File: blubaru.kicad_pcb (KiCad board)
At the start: 2 copper layers, 64 parts, among them IC1 ATTINY4313-P, J1 DB15, J2 DB15, J3 TS5A22364-Q1, J4 TS5A22364-Q1, J5 RN52_BREAKOUT, J6 JACK_TRS_5PINS, J7 DRV632, J8 JACK_TRS_5PINS, P1 CONN_01X06, P2 CONN_02X03, SW1 SW_Push, U1 DG419, U2 LD1117V33, Y1 11.0592MHz

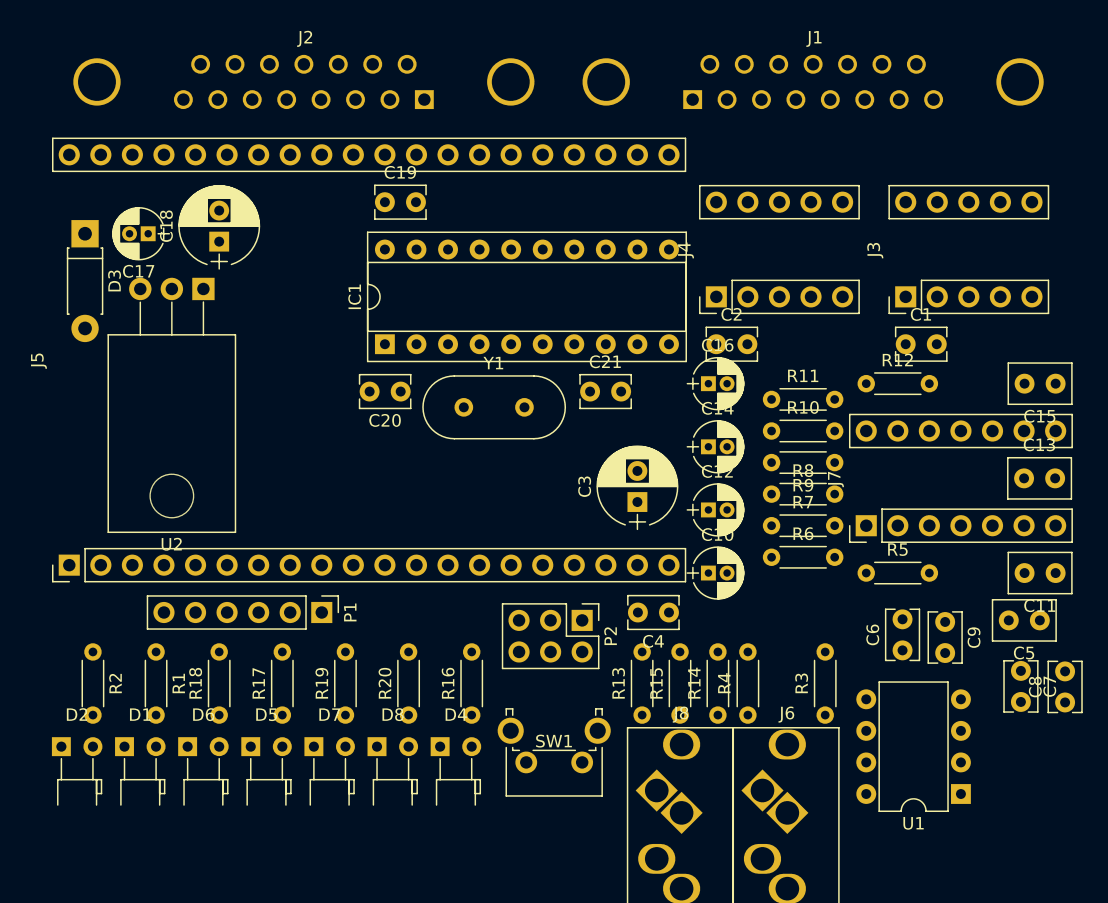
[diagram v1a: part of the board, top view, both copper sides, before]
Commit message: Add a better footprint for the regulator
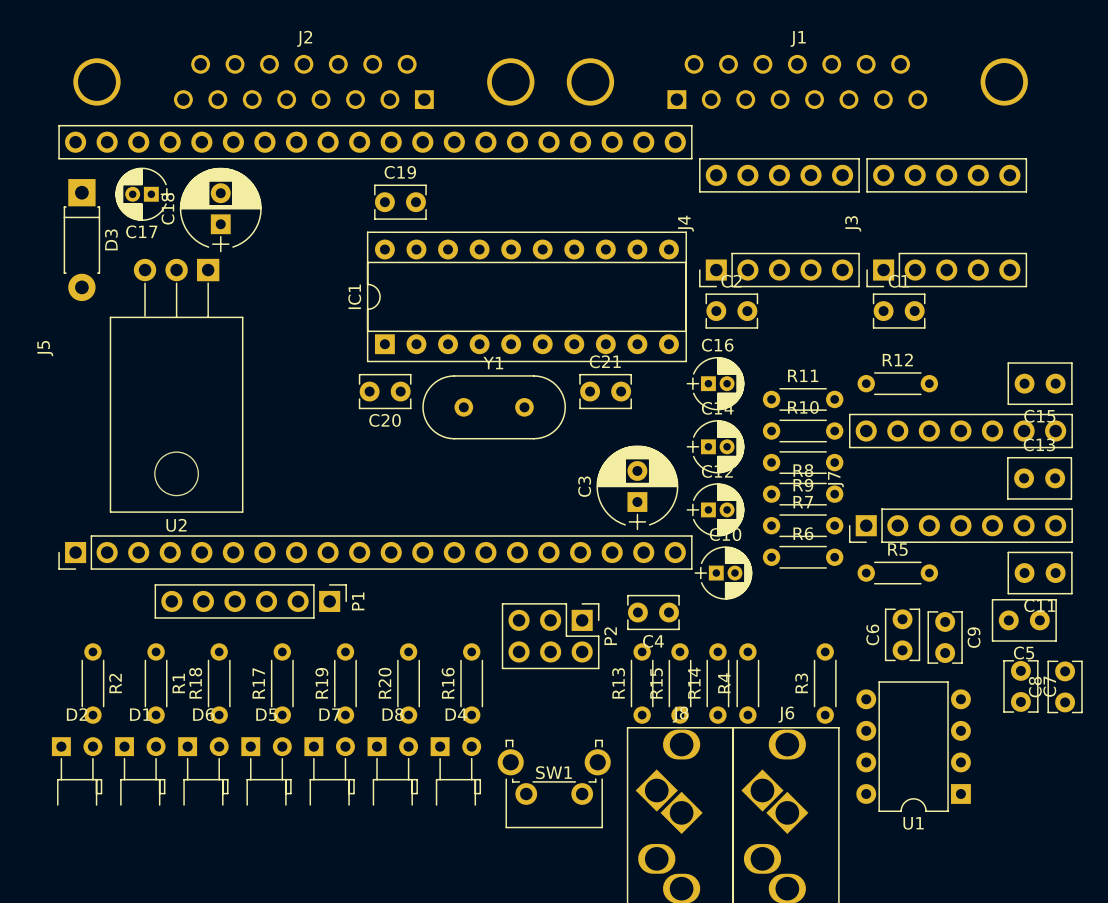
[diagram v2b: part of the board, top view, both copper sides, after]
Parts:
- U2: footprint TO_SOT_Packages_THT:TO-220_Horizontal -> blubaru:TO-220_Horizontal
- moved D3 3.31 mm to (109.6, 79.9)
- moved C1 3.21 mm to (174.1, 89.4)
- moved C17 3.19 mm to (115.2, 80.0)
- moved J3 2.80 mm to (174.1, 82.3)
- moved C2 2.67 mm to (160.7, 89.4)
- moved SW1 2.54 mm to (149.9, 128.3)
- moved J4 2.16 mm to (160.7, 82.3)
- moved U2 1.57 mm to (119.8, 86.1)
- moved C18 1.40 mm to (120.8, 82.4)
- moved J1 1.27 mm to (157.5, 72.4)
- moved J5 1.14 mm to (109.1, 92.3)
- moved P1 1.09 mm to (129.5, 112.8)
- moved C10 0.63 mm to (160.7, 110.5)
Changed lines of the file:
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@@
   )
   (module blubaru:C_Disc_D4.0mm_W2.6mm_P2.50mm (layer Top)
-    (at 175.895 92.075)
+    (at 174.117 89.408)
     (descr "C, Disc series, Radial, pin pitch=2.50mm, , diameter*width=4.0*2.6mm^2, Capacitor, https://www.vishay.com/docs/45171/kseries.pdf")
     (tags "C Disc series Radial pin pitch 2.50mm  diameter 4.0mm width 2.6mm Capacitor")
@@
   )
   (module blubaru:C_Disc_D4.0mm_W2.6mm_P2.50mm (layer Top)
-    (at 160.655 92.075)
+    (at 160.655 89.408)
     (descr "C, Disc series, Radial, pin pitch=2.50mm, , diameter*width=4.0*2.6mm^2, Capacitor, https://www.vishay.com/docs/45171/kseries.pdf")
     (tags "C Disc series Radial pin pitch 2.50mm  diameter 4.0mm width 2.6mm Capacitor")
@@
   )
   (module blubaru:CP_Radial_D4.0mm_P1.50mm (layer Top)
-    (at 160.02 110.49)
+    (at 160.655 110.49)
     (descr "CP, Radial series, Radial, pin pitch=1.50mm, , diameter=4mm, Electrolytic Capacitor http://www.nichicon.co.jp/english/products/pdfs/e-usw.pdf")
     (tags "CP Radial series Radial pin pitch 1.50mm  diameter 4mm Electrolytic Capacitor")
@@
   )
   (module blubaru:CP_Radial_D4.0mm_P1.50mm (layer Top)
-    (at 114.935 83.185 180)
+    (at 115.189 80.01 180)
     (descr "CP, Radial series, Radial, pin pitch=1.50mm, , diameter=4mm, Electrolytic Capacitor http://www.nichicon.co.jp/english/products/pdfs/e-usw.pdf")
     (tags "CP Radial series Radial pin pitch 1.50mm  diameter 4mm Electrolytic Capacitor")
@@
   )
   (module blubaru:CP_Radial_D6.3mm_P2.50mm (layer Top)
-    (at 120.65 83.82 90)
+    (at 120.777 82.423 90)
     (descr "CP, Radial series, Radial, pin pitch=2.50mm, , diameter=6.3mm, Electrolytic Capacitor http://www.nichicon.co.jp/english/products/pdfs/e-usw.pdf")
     (tags "CP Radial series Radial pin pitch 2.50mm  diameter 6.3mm Electrolytic Capacitor")
@@
   )
   (module Diodes_THT:D_DO-41_SOD81_P7.62mm_Horizontal (layer Top)
-    (at 109.855 83.185 270)
+    (at 109.601 79.883 270)
     (descr "D, DO-41_SOD81 series, Axial, Horizontal, pin pitch=7.62mm, , length*diameter=5.2*2.7mm^2, , http://www.diodes.com/_files/packages/DO-41%20(Plastic).pdf")
     (tags "D DO-41_SOD81 series Axial Horizontal pin pitch 7.62mm  length 5.2mm diameter 2.7mm")
@@
   )
   (module blubaru:DB15FC (layer Top)
-    (at 158.75 72.39)
+    (at 157.48 72.39)
     (descr http://media.digikey.com/pdf/Data%20Sheets/Assmann%20PDFs/A-Dx%20-xx-A_KG-T4_T2_Dwg.pdf)
     (tags "CONN DB15")
@@
   )
   (module blubaru:TS5A22364-Q1 (layer Top)
-    (at 175.895 84.455 90)
+    (at 174.117 82.296 90)
     (descr "TS5A22364-Q1, http://www.proto-advantage.com/store/datasheets/PA0027.pdf")
     (tags "MSOP-10 to DIP-10 SMT Adapter")
@@
   )
   (module blubaru:TS5A22364-Q1 (layer Top)
-    (at 160.655 84.455 90)
+    (at 160.655 82.296 90)
     (descr "TS5A22364-Q1, http://www.proto-advantage.com/store/datasheets/PA0027.pdf")
     (tags "MSOP-10 to DIP-10 SMT Adapter")
@@
   )
   (module blubaru:RN52_Breakout (layer Top)
-    (at 108.585 93.345 90)
+    (at 109.093 92.329 90)
     (descr "RN52 Breakout, https://cdn.sparkfun.com/datasheets/Wireless/Bluetooth/RN-52%20Breakout_v11.pdf")
     (tags "RN52 Breakout")
@@
   )
   (module Pin_Headers:Pin_Header_Straight_1x06_Pitch2.54mm (layer Top)
-    (at 128.905 113.665 270)
+    (at 129.54 112.776 270)
     (descr "Through hole straight pin header, 1x06, 2.54mm pitch, single row")
     (tags "Through hole pin header THT 1x06 2.54mm single row")
@@
     )
   )
-  (module TO_SOT_Packages_THT:TO-220_Horizontal (layer Top)
-    (at 119.38 87.63 180)
-    (descr "TO-220, Horizontal, RM 2.54mm")
-    (tags "TO-220 Horizontal RM 2.54mm")
-    (fp_text reference U2 (at 2.54 -20.58 180) (layer F.SilkS)
-      (effects (font (size 1 1) (thickness 0.15)))
-    )
-    (fp_text value LD1117V33 (at 2.54 1.9 180) (layer F.Fab)
-      (effects (font (size 1 1) (thickness 0.15)))
-    )
-    (fp_text user %R (at 2.54 -20.58 180) (layer F.Fab)
-      (effects (font (size 1 1) (thickness 0.15)))
-    )
-    (fp_line (start -2.46 -13.06) (end -2.46 -19.46) (layer F.Fab) (width 0.1))
-    (fp_line (start -2.46 -19.46) (end 7.54 -19.46) (layer F.Fab) (width 0.1))
-    (fp_line (start 7.54 -19.46) (end 7.54 -13.06) (layer F.Fab) (width 0.1))
-    (fp_line (start 7.54 -13.06) (end -2.46 -13.06) (layer F.Fab) (width 0.1))
-    (fp_line (start -2.46 -3.81) (end -2.46 -13.06) (layer F.Fab) (width 0.1))
-    (fp_line (start -2.46 -13.06) (end 7.54 -13.06) (layer F.Fab) (width 0.1))
-    (fp_line (start 7.54 -13.06) (end 7.54 -3.81) (layer F.Fab) (width 0.1))
-    (fp_line (start 7.54 -3.81) (end -2.46 -3.81) (layer F.Fab) (width 0.1))
-    (fp_line (start 0 -3.81) (end 0 0) (layer F.Fab) (width 0.1))
-    (fp_line (start 2.54 -3.81) (end 2.54 0) (layer F.Fab) (width 0.1))
-    (fp_line (start 5.08 -3.81) (end 5.08 0) (layer F.Fab) (width 0.1))
-    (fp_line (start -2.58 -3.69) (end 7.66 -3.69) (layer F.SilkS) (width 0.12))
-    (fp_line (start -2.58 -19.58) (end 7.66 -19.58) (layer F.SilkS) (width 0.12))
-    (fp_line (start -2.58 -19.58) (end -2.58 -3.69) (layer F.SilkS) (width 0.12))
-    (fp_line (start 7.66 -19.58) (end 7.66 -3.69) (layer F.SilkS) (width 0.12))
-    (fp_line (start 0 -3.69) (end 0 -1.05) (layer F.SilkS) (width 0.12))
-    (fp_line (start 2.54 -3.69) (end 2.54 -1.066) (layer F.SilkS) (width 0.12))
-    (fp_line (start 5.08 -3.69) (end 5.08 -1.066) (layer F.SilkS) (width 0.12))
-    (fp_line (start -2.71 -19.71) (end -2.71 1.15) (layer F.CrtYd) (width 0.05))
-    (fp_line (start -2.71 1.15) (end 7.79 1.15) (layer F.CrtYd) (width 0.05))
-    (fp_line (start 7.79 1.15) (end 7.79 -19.71) (layer F.CrtYd) (width 0.05))
-    (fp_line (start 7.79 -19.71) (end -2.71 -19.71) (layer F.CrtYd) (width 0.05))
-    (fp_circle (center 2.54 -16.66) (end 4.39 -16.66) (layer F.Fab) (width 0.1))
-    (pad 0 np_thru_hole oval (at 2.54 -16.66 180) (size 3.5 3.5) (drill 3.5) (layers *.Cu *.Mask))
-    (pad 1 thru_hole rect (at 0 0 180) (size 1.8 1.8) (drill 1) (layers *.Cu *.Mask)
-      (net 1 GND))
-    (pad 2 thru_hole oval (at 2.54 0 180) (size 1.8 1.8) (drill 1) (layers *.Cu *.Mask)
-      (net 2 VCC))
-    (pad 3 thru_hole oval (at 5.08 0 180) (size 1.8 1.8) (drill 1) (layers *.Cu *.Mask)
-      (net 49 "Net-(C17-Pad1)"))
-    (model ${KISYS3DMOD}/TO_SOT_Packages_THT.3dshapes/TO-220_Horizontal.wrl
-      (at (xyz 0.1 0 0))
-      (scale (xyz 0.393701 0.393701 0.393701))
-      (rotate (xyz 0 0 0))
-    )
-  )
   (module Crystals:Crystal_HC49-4H_Vertical (layer Top)
     (at 140.335 97.155)
@@
   )
   (module blubaru:SW_Tactile_SPST_Angled_PTS645Vx58-2LFS (layer Top)
-    (at 149.86 125.73 180)
+    (at 149.86 128.27 180)
     (descr "tactile switch SPST right angle, PTS645VL58-2 LFS")
     (tags "tactile switch SPST angled PTS645VL58-2 LFS C&K Button")
@@
       (rotate (xyz 0 0 0))
     )
+  )
+  (module blubaru:TO-220_Horizontal (layer Top)
+    (at 119.761 86.106 180)
+    (descr "TO-220, Horizontal, RM 2.54mm")
+    (tags "TO-220 Horizontal RM 2.54mm")
+    (fp_text reference U2 (at 2.54 -20.58 180) (layer F.SilkS)
+      (effects (font (size 1 1) (thickness 0.15)))
+    )
+    (fp_text value LD1117V33 (at 2.54 1.9 180) (layer F.Fab)
+      (effects (font (size 1 1) (thickness 0.15)))
+    )
+    (fp_text user %R (at 2.54 -20.58 180) (layer F.Fab)
+      (effects (font (size 1 1) (thickness 0.15)))
+    )
+    (fp_line (start -2.66 -13.06) (end -2.66 -19.35) (layer F.Fab) (width 0.1))
+    (fp_line (start -2.66 -19.35) (end 7.74 -19.35) (layer F.Fab) (width 0.1))
+    (fp_line (start 7.74 -19.35) (end 7.74 -13.06) (layer F.Fab) (width 0.1))
+    (fp_line (start -2.66 -3.93) (end -2.66 -13.06) (layer F.Fab) (width 0.1))
+    (fp_line (start -2.66 -12.95) (end 7.74 -12.95) (layer F.Fab) (width 0.1))
+    (fp_line (start 7.74 -13.06) (end 7.74 -3.93) (layer F.Fab) (width 0.1))
+    (fp_line (start 7.74 -3.93) (end -2.66 -3.93) (layer F.Fab) (width 0.1))
+    (fp_line (start 0 -3.93) (end 0 0) (layer F.Fab) (width 0.1))
+    (fp_line (start 2.54 -3.93) (end 2.54 0) (layer F.Fab) (width 0.1))
+    (fp_line (start 5.08 -3.93) (end 5.08 0) (layer F.Fab) (width 0.1))
+    (fp_line (start -2.78 -3.81) (end 7.86 -3.81) (layer F.SilkS) (width 0.12))
+    (fp_line (start -2.78 -19.48) (end 7.86 -19.48) (layer F.SilkS) (width 0.12))
+    (fp_line (start -2.78 -19.47) (end -2.78 -3.81) (layer F.SilkS) (width 0.12))
+    (fp_line (start 7.86 -19.47) (end 7.86 -3.81) (layer F.SilkS) (width 0.12))
+    (fp_line (start 0 -3.81) (end 0 -1.05) (layer F.SilkS) (width 0.12))
+    (fp_line (start 2.54 -3.81) (end 2.54 -1.066) (layer F.SilkS) (width 0.12))
+    (fp_line (start 5.08 -3.69) (end 5.08 -1.066) (layer F.SilkS) (width 0.12))
+    (fp_line (start -2.91 -19.6) (end -2.91 1.15) (layer F.CrtYd) (width 0.05))
+    (fp_line (start -2.91 1.15) (end 7.99 1.15) (layer F.CrtYd) (width 0.05))
+    (fp_line (start 7.99 1.15) (end 7.99 -19.6) (layer F.CrtYd) (width 0.05))
+    (fp_line (start 7.99 -19.61) (end -2.91 -19.61) (layer F.CrtYd) (width 0.05))
+    (fp_circle (center 2.54 -16.4) (end 4.39 -16.66) (layer F.Fab) (width 0.1))
+    (pad "" np_thru_hole oval (at 2.54 -16.4 180) (size 3.5 3.5) (drill 3.5) (layers *.Cu *.Mask))
+    (pad 1 thru_hole rect (at 0 0 180) (size 1.8 1.8) (drill 1) (layers *.Cu *.Mask)
+      (net 1 GND))
+    (pad 2 thru_hole oval (at 2.54 0 180) (size 1.8 1.8) (drill 1) (layers *.Cu *.Mask)
+      (net 2 VCC))
+    (pad 3 thru_hole oval (at 5.08 0 180) (size 1.8 1.8) (drill 1) (layers *.Cu *.Mask)
+      (net 49 "Net-(C17-Pad1)"))
+    (model ${KISYS3DMOD}/TO_SOT_Packages_THT.3dshapes/TO-220_Horizontal.wrl
+      (at (xyz 0.1 0 0))
+      (scale (xyz 0.393701 0.393701 0.393701))
+      (rotate (xyz 0 0 0))
+    )

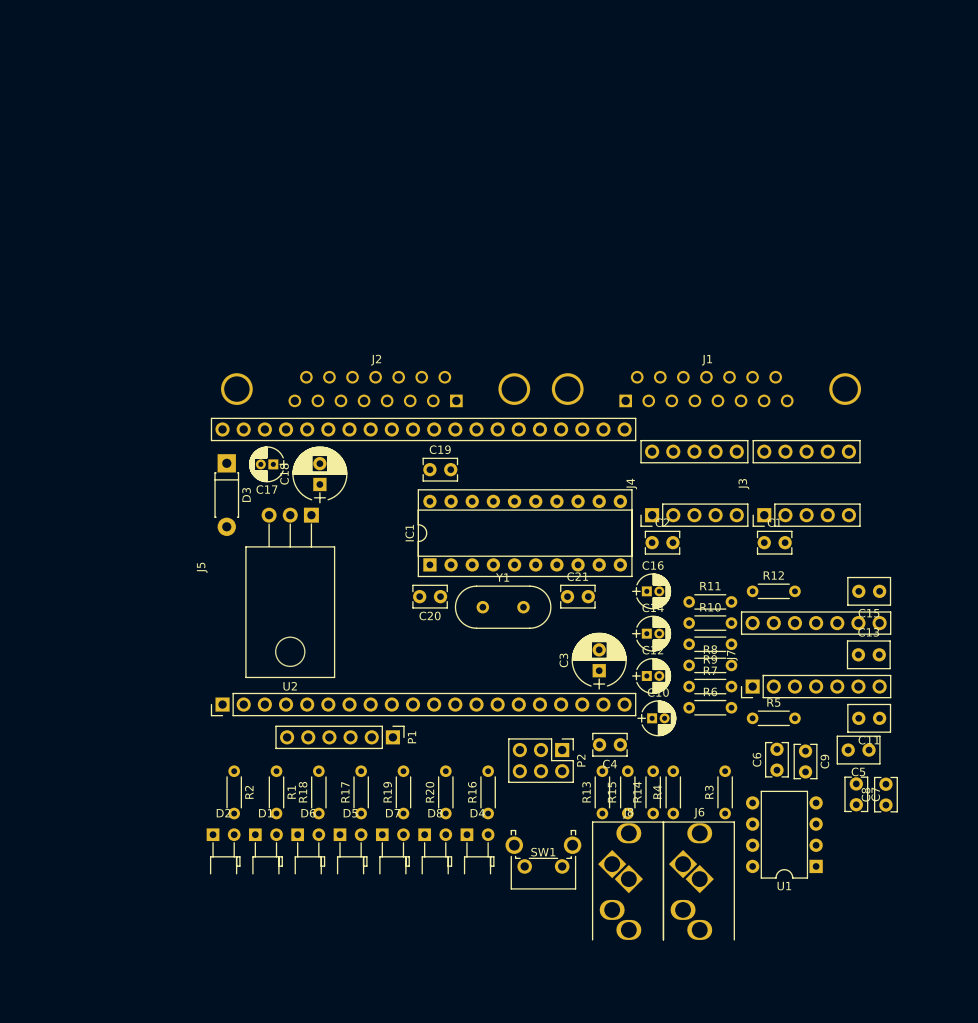
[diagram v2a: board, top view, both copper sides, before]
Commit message: Rough layout with short audio path.
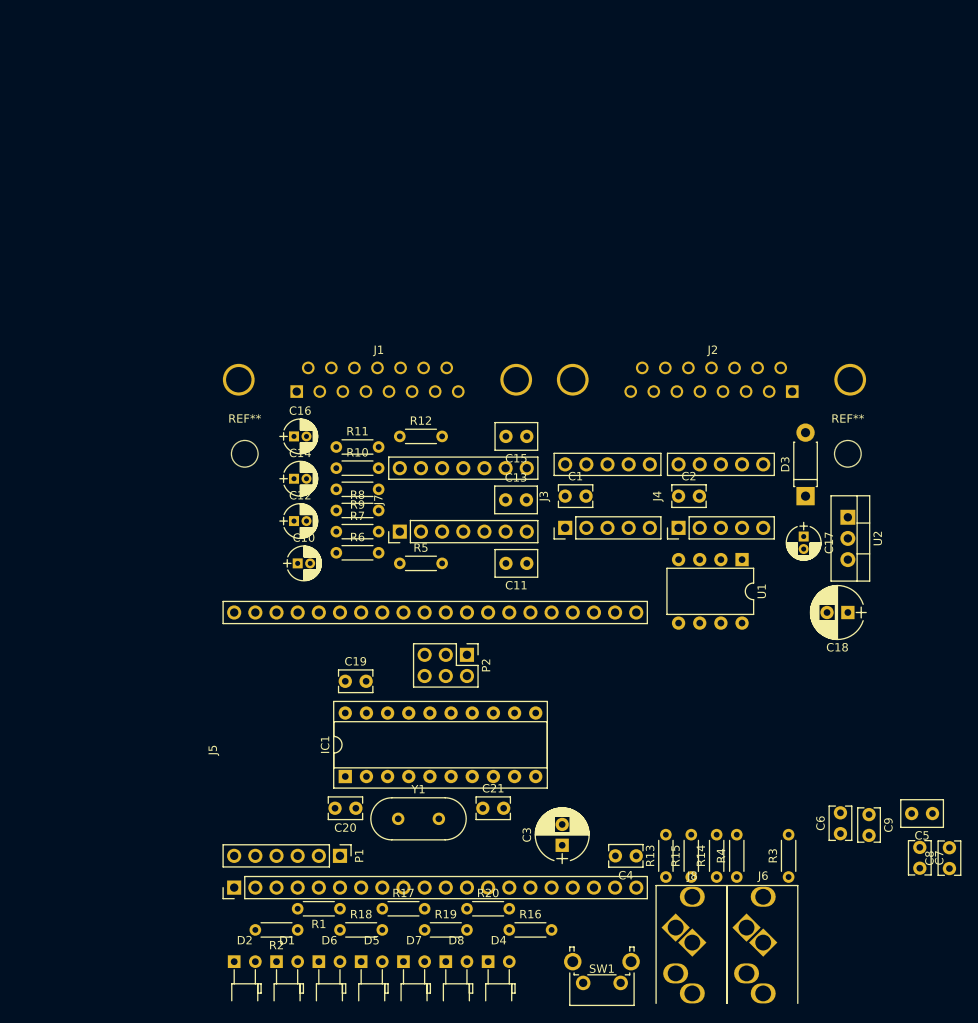
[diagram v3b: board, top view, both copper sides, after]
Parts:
- added REF**: MountingHole_3.2mm_M3, Mounting_Holes:MountingHole_3.2mm_M3, F.Cu at (184.2, 78.7)
- added REF**: MountingHole_3.2mm_M3, Mounting_Holes:MountingHole_3.2mm_M3, F.Cu at (111.8, 78.7)
- U2: footprint blubaru:TO-220_Horizontal -> TO_SOT_Packages_THT:TO-220-3_Vertical
- moved D3 69.6 mm to (179.1, 83.8), turned to 90 degrees
- moved C18 65.2 mm to (184.2, 97.8), turned to 180 degrees
- moved U2 64.4 mm to (184.2, 86.4), turned to 270 degrees
- moved C17 64.2 mm to (178.8, 88.7), turned to 270 degrees
- moved C10 46.4 mm to (118.1, 91.9)
- moved C11 46.3 mm to (145.6, 91.9)
- moved C15 46.3 mm to (145.6, 76.7)
- moved C12 46.3 mm to (117.7, 86.8)
- moved C14 46.3 mm to (117.7, 81.7)
- moved C16 46.3 mm to (117.7, 76.7)
- moved R9 46.3 mm to (127.8, 83.0)
- moved R7 46.3 mm to (122.7, 88.1)
- moved C13 46.3 mm to (143.1, 84.3)
- moved J7 46.3 mm to (130.4, 84.3)
- moved R10 46.3 mm to (122.7, 80.5)
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
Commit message: Update layout with new netlist
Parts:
- IC1: footprint Housings_DIP:DIP-20_W7.62mm_Socket -> blubaru:DIP-20_W7.62mm_Socket
- U2: footprint TO_SOT_Packages_THT:TO-220-3_Vertical -> TO_SOT_Packages_THT:TO-220_Vertical

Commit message: First feasible layout.
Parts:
- added REF**: MountingHole_3.2mm_M3, Mounting_Holes:MountingHole_3.2mm_M3, F.Cu at (184.2, 135.9)
- added REF**: MountingHole_3.2mm_M3, Mounting_Holes:MountingHole_3.2mm_M3, F.Cu at (111.8, 135.9)
- moved R18 37.3 mm to (132.1, 99.7), turned to 270 degrees
- moved P2 35.6 mm to (174.0, 104.8)
- moved R17 34.2 mm to (134.6, 99.7), turned to 270 degrees
- moved C5 29.9 mm to (165.1, 115.6), turned to 90 degrees
- moved C8 27.9 mm to (169.5, 120.7)
- moved C7 27.1 mm to (168.9, 113.1)
- moved C9 26.9 mm to (161.3, 113.1)
- moved C6 22.9 mm to (160.7, 120.7)
- moved R19 17.5 mm to (146.1, 123.8), turned to 90 degrees
- moved R2 16.2 mm to (111.1, 121.3), turned to 270 degrees
- moved R1 15.4 mm to (113.7, 121.3), turned to 270 degrees
- moved R15 15.1 mm to (179.1, 123.2)
- moved R13 13.3 mm to (174.0, 123.2)
- moved R3 12.4 mm to (166.4, 123.2)
- moved J8 11.7 mm to (176.0, 138.3)
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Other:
- board outline added: 80 x 78.7 mm
